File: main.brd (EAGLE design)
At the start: 31.4 x 34.3 mm, 14 parts, among them IC1 TL071P

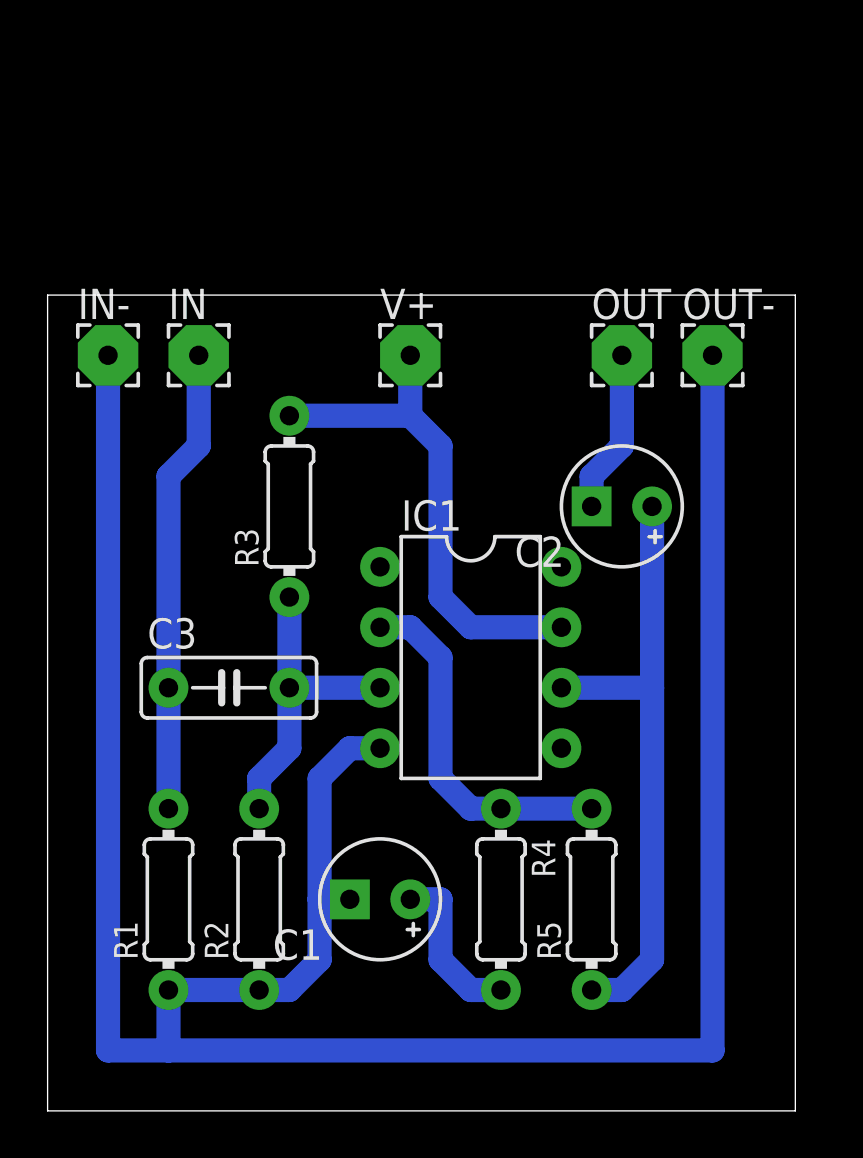
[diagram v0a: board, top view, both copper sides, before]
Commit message: Convert to smd.
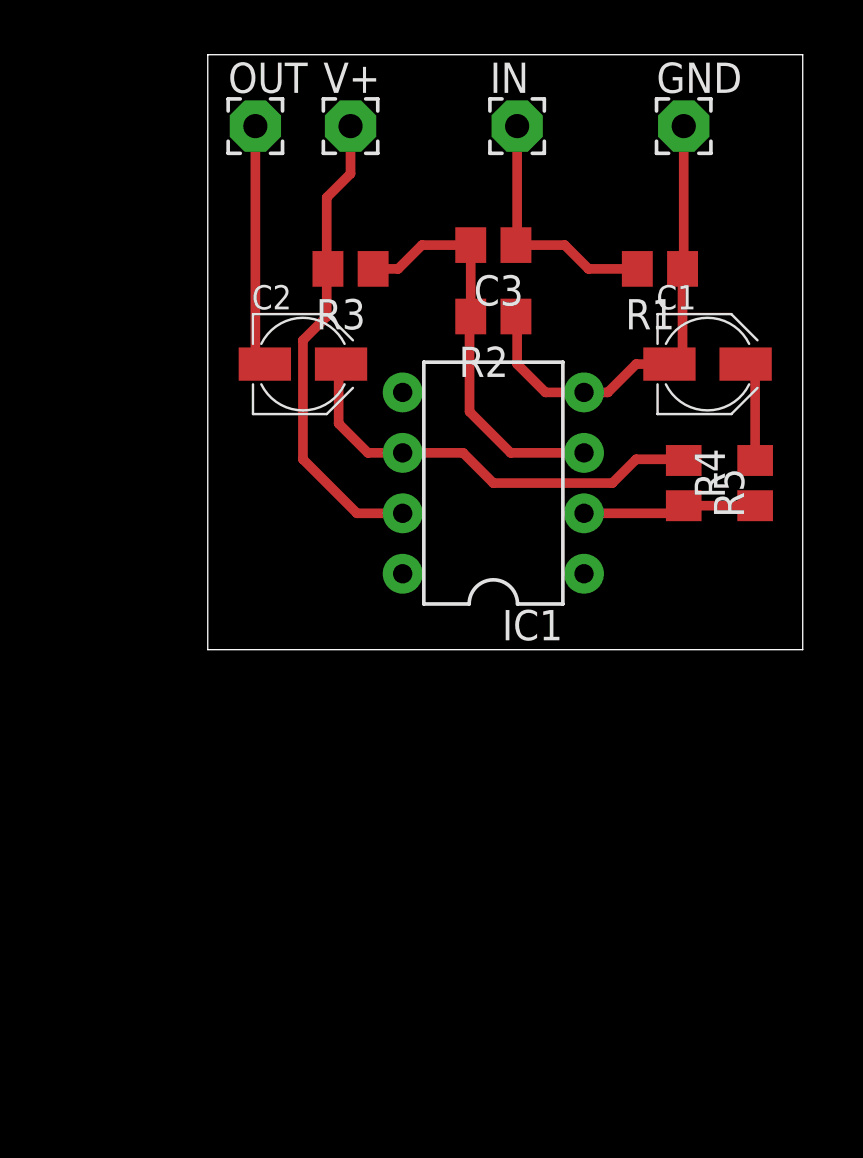
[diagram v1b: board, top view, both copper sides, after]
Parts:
- removed IN-, OUT-: (no value), wirepad:2,54/0,8
- added GND: WIREPAD2,15/1,0, wirepad:2,15/1,0
- C1, C2: device rcl:E2,5-5 -> rcl:PANASONIC_B
- C3: device rcl:C050-025X075 -> rcl:C0805
- IN, OUT, V+: value (none) -> WIREPAD2,15/1,0; device wirepad:2,54/0,8 -> wirepad:2,15/1,0
- R1, R2, R3, R4, R5: device resistor:0204/7 -> rcl:R0805
- moved R1 33.6 mm to (27.0, 43.0), turned to 180 degrees
- moved R2 26.4 mm to (20.0, 41.0), turned to 180 degrees
- moved C1 26.4 mm to (29.0, 39.0), turned to 0 degrees
- moved C3 21.7 mm to (20.0, 44.0), turned to 180 degrees
- moved R4 20.5 mm to (31.0, 34.0), turned to 90 degrees
- moved OUT 18.2 mm to (10.0, 49.0)
- moved R5 17.9 mm to (28.0, 34.0), turned to 270 degrees
- moved IN 16.5 mm to (21.0, 49.0)
- moved C2 14.7 mm to (12.0, 39.0), turned to 0 degrees
- moved R3 10.3 mm to (14.0, 43.0), turned to 180 degrees
- moved V+ 9.95 mm to (14.0, 49.0)
- moved IC1 7.39 mm to (20.0, 34.0), turned to 90 degrees
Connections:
- net GND: now also GND.1; no longer IN-.1, OUT-.1
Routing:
- net GND: track 105.2 -> 19.7 mm
- net N$7: track 19.6 -> 10.6 mm
- net N$4: track 15.0 -> 7.32 mm
- net N$5: track 25.9 -> 18.5 mm
- net N$1: track 13.2 -> 17.1 mm
- net N$2: track 6.88 -> 10.2 mm
- net N$3: track 6.88 -> 4.22 mm
- net N$6: track 21.4 -> 20.0 mm
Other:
- board size 31.4 x 34.3 mm -> 25 x 25 mm

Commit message: Clean up traces.
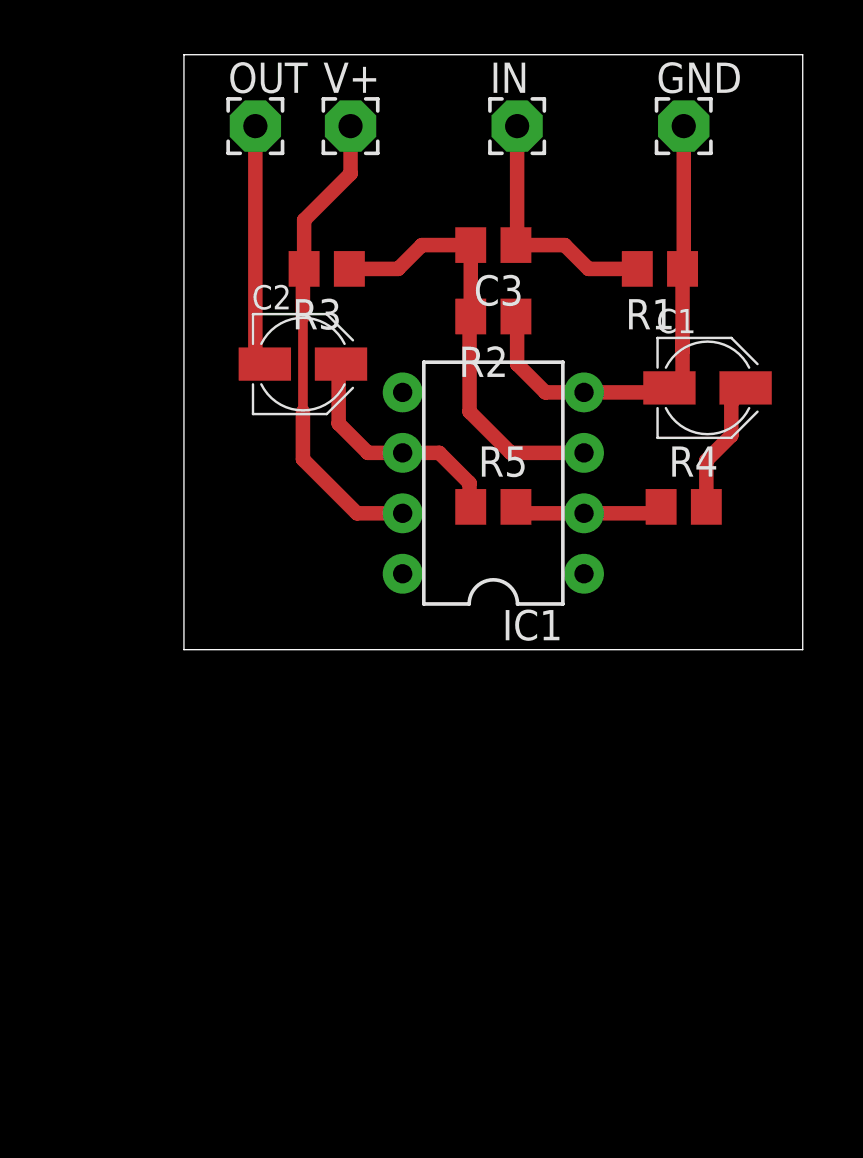
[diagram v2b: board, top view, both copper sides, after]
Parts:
- moved R5 8.06 mm to (20.0, 33.0), turned to 0 degrees
- moved R4 3.16 mm to (28.0, 33.0), turned to 0 degrees
- moved C1 1.00 mm to (29.0, 38.0)
- moved R3 1.00 mm to (13.0, 43.0)
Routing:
- net N$5: track 18.5 -> 10.1 mm
- net N$3: track 4.22 -> 5.68 mm
- net N$1: track 17.1 -> 18.1 mm
- net N$4: track 7.32 -> 6.32 mm
- net GND: track 19.7 -> 20.5 mm
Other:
- board size 25 x 25 mm -> 26 x 25 mm

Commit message: Add ground fill.
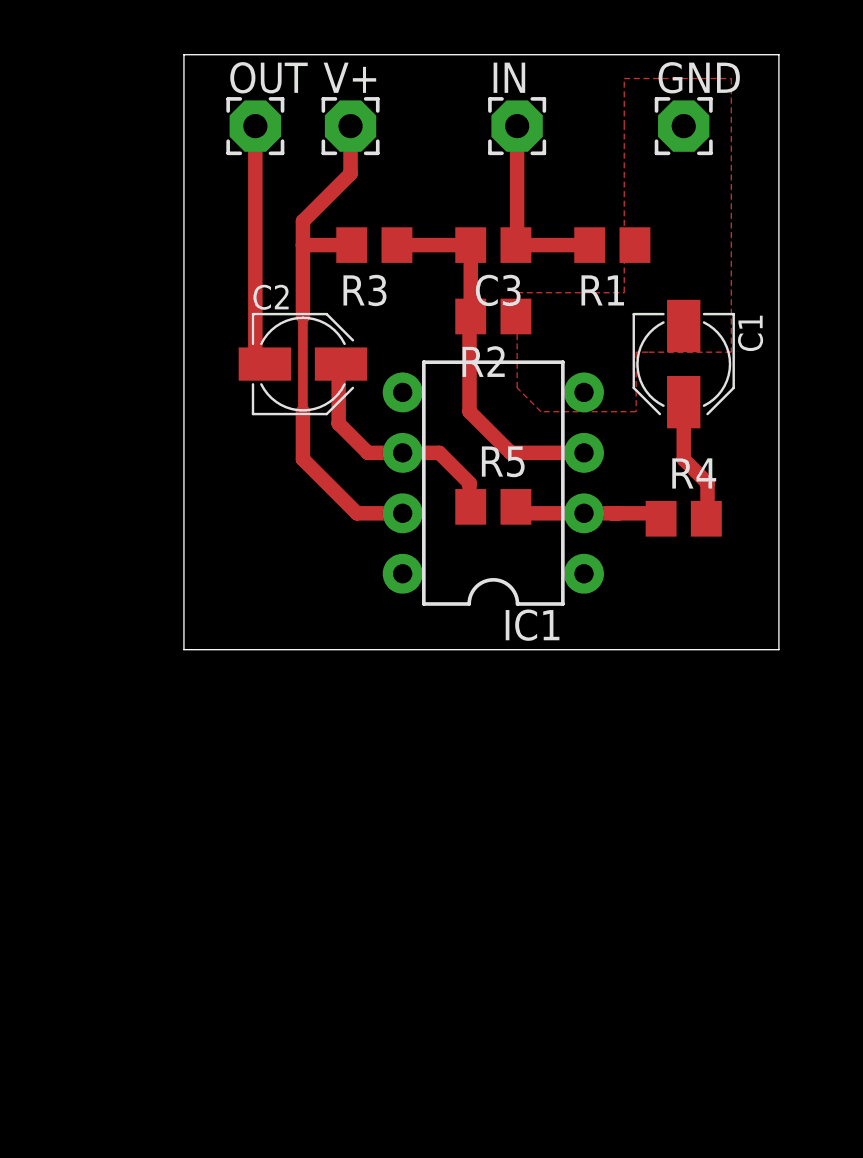
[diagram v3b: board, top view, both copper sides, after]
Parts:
- moved R1 2.24 mm to (25.0, 44.0)
- moved R3 2.24 mm to (15.0, 44.0)
- moved C1 1.41 mm to (28.0, 39.0), turned to 270 degrees
- moved R4 0.50 mm to (28.0, 32.5)
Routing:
- net GND: track 20.5 -> 0.07 mm
- net N$7: track 10.6 -> 8.12 mm
- net N$1: track 18.1 -> 15.6 mm
- net N$6: track 20.1 -> 22.0 mm
- added copper zone on layer 1, net GND
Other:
- board size 26 x 25 mm -> 25 x 25 mm
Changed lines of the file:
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@@
 <board>
 <plain>
-<wire x1="7" y1="27" x2="33" y2="27" width="0" layer="20"/>
-<wire x1="33" y1="27" x2="33" y2="52" width="0" layer="20"/>
-<wire x1="33" y1="52" x2="7" y2="52" width="0" layer="20"/>
+<wire x1="7" y1="27" x2="32" y2="27" width="0" layer="20"/>
+<wire x1="32" y1="27" x2="32" y2="52" width="0" layer="20"/>
+<wire x1="32" y1="52" x2="7" y2="52" width="0" layer="20"/>
 <wire x1="7" y1="52" x2="7" y2="27" width="0" layer="20"/>
 </plain>
@@
 </autorouter>
 <elements>
-<element name="C1" library="rcl" package="PANASONIC_B" value="10u" x="29" y="38"/>
+<element name="C1" library="rcl" package="PANASONIC_B" value="10u" x="28" y="39" rot="R270"/>
 <element name="C2" library="rcl" package="PANASONIC_B" value="10uf" x="12" y="39"/>
 <element name="C3" library="rcl" package="C0805" value="100n" x="20" y="44" rot="R180"/>
@@
 <element name="GND" library="wirepad" package="2,15/1,0" value="WIREPAD2,15/1,0" x="28" y="49"/>
 <element name="OUT" library="wirepad" package="2,15/1,0" value="WIREPAD2,15/1,0" x="10" y="49"/>
-<element name="R1" library="rcl" package="R0805" value="1M" x="27" y="43" rot="R180"/>
+<element name="R1" library="rcl" package="R0805" value="1M" x="25" y="44" rot="R180"/>
 <element name="R2" library="rcl" package="R0805" value="1M" x="20" y="41" rot="R180"/>
-<element name="R3" library="rcl" package="R0805" value="1M" x="13" y="43" rot="R180"/>
-<element name="R4" library="rcl" package="R0805" value="100k" x="28" y="33"/>
+<element name="R3" library="rcl" package="R0805" value="1M" x="15" y="44" rot="R180"/>
+<element name="R4" library="rcl" package="R0805" value="100k" x="28" y="32.5"/>
 <element name="R5" library="rcl" package="R0805" value="220k" x="20" y="33"/>
 <element name="V+" library="wirepad" package="2,15/1,0" value="WIREPAD2,15/1,0" x="14" y="49"/>
@@
 <wire x1="19" y1="37" x2="19" y2="40.95" width="0.6096" layer="1"/>
 <wire x1="19.05" y1="41" x2="19" y2="40.95" width="0.4064" layer="1"/>
-<wire x1="13.95" y1="43" x2="16" y2="43" width="0.6096" layer="1"/>
-<wire x1="16" y1="43" x2="17" y2="44" width="0.6096" layer="1"/>
-<wire x1="17" y1="44" x2="19.05" y2="44" width="0.6096" layer="1"/>
+<wire x1="15.95" y1="44" x2="19.05" y2="44" width="0.6096" layer="1"/>
 <wire x1="19.05" y1="44" x2="19.05" y2="41" width="0.6096" layer="1"/>
 </signal>
@@
 <contactref element="C1" pad="+"/>
 <contactref element="R4" pad="2"/>
-<wire x1="28.95" y1="33" x2="28.95" y2="34.95" width="0.6096" layer="1"/>
-<wire x1="28.95" y1="34.95" x2="30" y2="36" width="0.6096" layer="1"/>
-<wire x1="30" y1="36" x2="30" y2="37.4" width="0.6096" layer="1"/>
-<wire x1="30" y1="37.4" x2="30.6" y2="38" width="0.6096" layer="1"/>
+<wire x1="28" y1="37.4" x2="28" y2="35" width="0.6096" layer="1"/>
+<wire x1="28" y1="35" x2="29" y2="34" width="0.6096" layer="1"/>
+<wire x1="29" y1="34" x2="29" y2="32.55" width="0.6096" layer="1"/>
+<wire x1="29" y1="32.55" x2="28.95" y2="32.5" width="0.6096" layer="1"/>
 </signal>
 <signal name="N$4">
@@
 <wire x1="21.22" y1="32.73" x2="23.81" y2="32.73" width="0.6096" layer="1"/>
 <wire x1="21.22" y1="32.73" x2="20.95" y2="33" width="0.6096" layer="1"/>
-<wire x1="23.81" y1="32.73" x2="26.78" y2="32.73" width="0.6096" layer="1"/>
-<wire x1="26.78" y1="32.73" x2="27.05" y2="33" width="0.6096" layer="1"/>
+<wire x1="23.81" y1="32.73" x2="25" y2="32.73" width="0.6096" layer="1"/>
+<wire x1="25" y1="32.73" x2="25.27" y2="32.73" width="0.6096" layer="1"/>
+<wire x1="25" y1="32.73" x2="27.05" y2="32.73" width="0.6096" layer="1"/>
+<wire x1="27.05" y1="32.73" x2="27.05" y2="32.5" width="0.6096" layer="1"/>
 </signal>
 <signal name="N$5">
@@
 <contactref element="C3" pad="1"/>
 <contactref element="IN" pad="1"/>
-<wire x1="20.95" y1="44" x2="23" y2="44" width="0.6096" layer="1"/>
-<wire x1="23" y1="44" x2="24" y2="43" width="0.6096" layer="1"/>
-<wire x1="26.05" y1="43" x2="24" y2="43" width="0.6096" layer="1"/>
-<wire x1="26" y1="43.05" x2="26.05" y2="43" width="0.4064" layer="1"/>
+<wire x1="24.05" y1="44" x2="20.95" y2="44" width="0.6096" layer="1"/>
 <wire x1="21" y1="49" x2="21" y2="44.05" width="0.6096" layer="1"/>
 <wire x1="21" y1="44.05" x2="20.95" y2="44" width="0.4064" layer="1"/>
@@
 <contactref element="IC1" pad="4"/>
 <contactref element="GND" pad="1"/>
-<wire x1="22.19" y1="37.81" x2="23.81" y2="37.81" width="0.6096" layer="1"/>
-<wire x1="22.19" y1="37.81" x2="21" y2="39" width="0.6096" layer="1"/>
-<wire x1="21" y1="40.95" x2="21" y2="39" width="0.6096" layer="1"/>
 <wire x1="20.95" y1="41" x2="21" y2="40.95" width="0.4064" layer="1"/>
-<wire x1="27.95" y1="43" x2="27.95" y2="39.55" width="0.6096" layer="1"/>
-<wire x1="28" y1="49" x2="28" y2="43.05" width="0.6096" layer="1"/>
-<wire x1="28" y1="43.05" x2="27.95" y2="43" width="0.4064" layer="1"/>
-<wire x1="23.81" y1="37.81" x2="27.21" y2="37.81" width="0.6096" layer="1"/>
-<wire x1="27.21" y1="37.81" x2="27.4" y2="38" width="0.6096" layer="1"/>
-<wire x1="27.95" y1="40" x2="27.95" y2="38.05" width="0.6096" layer="1"/>
-<wire x1="27.95" y1="38.05" x2="28" y2="38" width="0.6096" layer="1"/>
-<wire x1="27.95" y1="40" x2="27.95" y2="39.55" width="0" layer="19" extent="1-1"/>
-<wire x1="27.4" y1="38" x2="27.95" y2="38.05" width="0" layer="19" extent="1-1"/>
+<polygon width="0.3048" layer="1">
+<vertex x="25.5" y="44"/>
+<vertex x="25.5" y="49"/>
+<vertex x="25.5" y="51"/>
+<vertex x="30" y="51"/>
+<vertex x="30" y="39.5"/>
+<vertex x="26.5" y="39.5"/>
+<vertex x="26" y="39.5"/>
+<vertex x="26" y="37"/>
+<vertex x="22" y="37"/>
+<vertex x="21" y="38"/>
+<vertex x="21" y="42"/>
+<vertex x="25.5" y="42"/>
+</polygon>
 </signal>
 <signal name="N$2">
@@
 <wire x1="16.19" y1="32.73" x2="14.27" y2="32.73" width="0.6096" layer="1"/>
 <wire x1="14.27" y1="32.73" x2="12" y2="35" width="0.6096" layer="1"/>
-<wire x1="12.05" y1="45.05" x2="12.05" y2="43" width="0.6096" layer="1"/>
-<wire x1="12.05" y1="45.05" x2="14" y2="47" width="0.6096" layer="1"/>
 <wire x1="14" y1="47" x2="14" y2="49" width="0.6096" layer="1"/>
-<wire x1="12" y1="42.95" x2="12.05" y2="43" width="0.4064" layer="1"/>
-<wire x1="12.05" y1="43" x2="12" y2="43" width="0.6096" layer="1"/>
-<wire x1="12" y1="41" x2="12" y2="43" width="0.6096" layer="1"/>
 <wire x1="12" y1="35" x2="12" y2="37" width="0.6096" layer="1"/>
 <wire x1="12" y1="37" x2="12" y2="41" width="0.4064" layer="1"/>
+<wire x1="12" y1="45" x2="14" y2="47" width="0.6096" layer="1"/>
+<wire x1="12" y1="44" x2="12" y2="41" width="0.6096" layer="1"/>
+<wire x1="12" y1="44" x2="12" y2="45" width="0.6096" layer="1"/>
+<wire x1="14.05" y1="44" x2="12" y2="44" width="0.6096" layer="1"/>
 </signal>
 </signals>

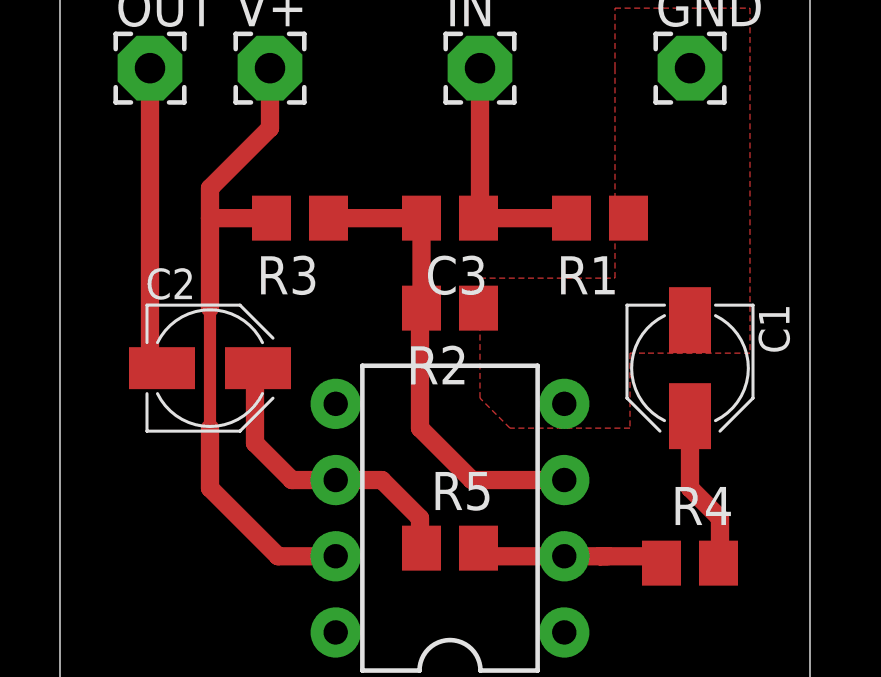
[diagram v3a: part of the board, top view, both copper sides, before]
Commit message: Add more clearance between cap and a dip socket.
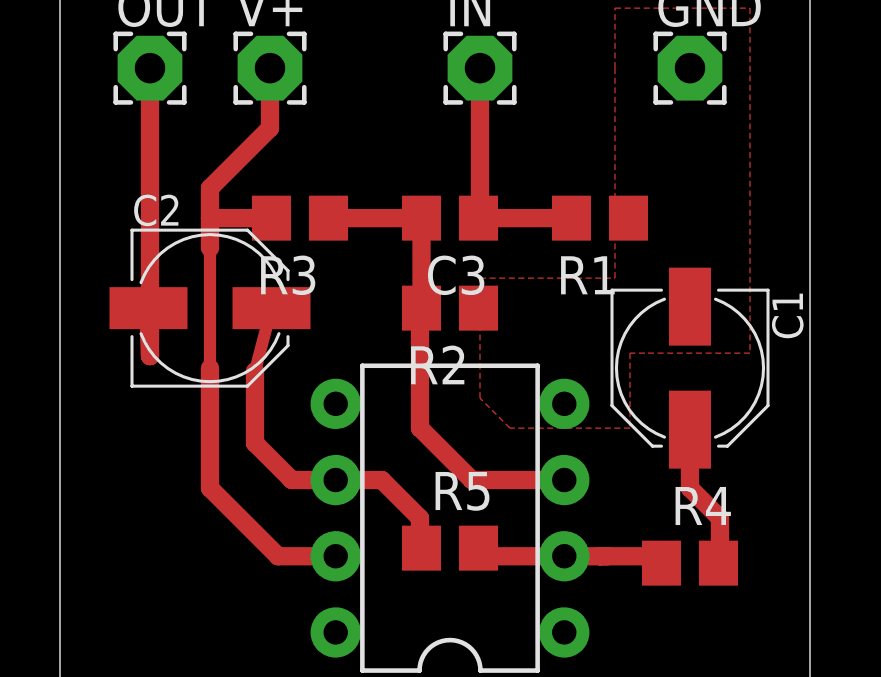
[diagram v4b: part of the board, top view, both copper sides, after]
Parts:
- C1, C2: device rcl:PANASONIC_B -> rcl:PANASONIC_C
- moved C2 2.00 mm to (12.0, 41.0)
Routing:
- net N$5: track 10.1 -> 12.1 mm
- net N$2: track 10.2 -> 11.2 mm
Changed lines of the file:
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@@
 </autorouter>
 <elements>
-<element name="C1" library="rcl" package="PANASONIC_B" value="10u" x="28" y="39" rot="R270"/>
-<element name="C2" library="rcl" package="PANASONIC_B" value="10uf" x="12" y="39"/>
+<element name="C1" library="rcl" package="PANASONIC_C" value="10u" x="28" y="39" rot="R270"/>
+<element name="C2" library="rcl" package="PANASONIC_C" value="10uf" x="12" y="41"/>
 <element name="C3" library="rcl" package="C0805" value="100n" x="20" y="44" rot="R180"/>
 <element name="IC1" library="linear" package="DIL08" value="TL071P" x="20" y="34" rot="R90"/>
@@
 <contactref element="C1" pad="+"/>
 <contactref element="R4" pad="2"/>
-<wire x1="28" y1="37.4" x2="28" y2="35" width="0.6096" layer="1"/>
+<wire x1="28" y1="36.95" x2="28" y2="35" width="0.6096" layer="1"/>
 <wire x1="28" y1="35" x2="29" y2="34" width="0.6096" layer="1"/>
 <wire x1="29" y1="34" x2="29" y2="32.55" width="0.6096" layer="1"/>
@@
 <wire x1="14.73" y1="35.27" x2="13.5" y2="36.5" width="0.6096" layer="1"/>
 <wire x1="13.5" y1="36.5" x2="13.5" y2="38.9" width="0.6096" layer="1"/>
-<wire x1="13.5" y1="38.9" x2="13.6" y2="39" width="0.4064" layer="1"/>
+<wire x1="13.5" y1="38.9" x2="14.05" y2="41" width="0.4064" layer="1"/>
 <wire x1="16.19" y1="35.27" x2="17.73" y2="35.27" width="0.6096" layer="1"/>
 <wire x1="17.73" y1="35.27" x2="19" y2="34" width="0.6096" layer="1"/>
@@
 <contactref element="OUT" pad="1"/>
 <wire x1="10" y1="49" x2="10" y2="39.4" width="0.6096" layer="1"/>
-<wire x1="10" y1="39.4" x2="10.4" y2="39" width="0.6096" layer="1"/>
+<wire x1="10" y1="39.4" x2="9.95" y2="41" width="0.6096" layer="1"/>
 </signal>
 <signal name="N$6">
@@
 <wire x1="14.27" y1="32.73" x2="12" y2="35" width="0.6096" layer="1"/>
 <wire x1="14" y1="47" x2="14" y2="49" width="0.6096" layer="1"/>
-<wire x1="12" y1="35" x2="12" y2="37" width="0.6096" layer="1"/>
-<wire x1="12" y1="37" x2="12" y2="41" width="0.4064" layer="1"/>
+<wire x1="12" y1="35" x2="12" y2="39" width="0.6096" layer="1"/>
+<wire x1="12" y1="39" x2="12" y2="43" width="0.4064" layer="1"/>
 <wire x1="12" y1="45" x2="14" y2="47" width="0.6096" layer="1"/>
-<wire x1="12" y1="44" x2="12" y2="41" width="0.6096" layer="1"/>
+<wire x1="12" y1="44" x2="12" y2="43" width="0.6096" layer="1"/>
 <wire x1="12" y1="44" x2="12" y2="45" width="0.6096" layer="1"/>
 <wire x1="14.05" y1="44" x2="12" y2="44" width="0.6096" layer="1"/>
